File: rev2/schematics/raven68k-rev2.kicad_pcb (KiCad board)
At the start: 2 copper layers, 70 parts, among them IC1 L5970D013TR, IC2 L5970D013TR, J1 CPLD_JTAG, J2 DUART_IO, U1 MCP100-465D, U10 28C256, U11 28C256, U2 68010D, U3 XC9572XL-TQ100, U4 68681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

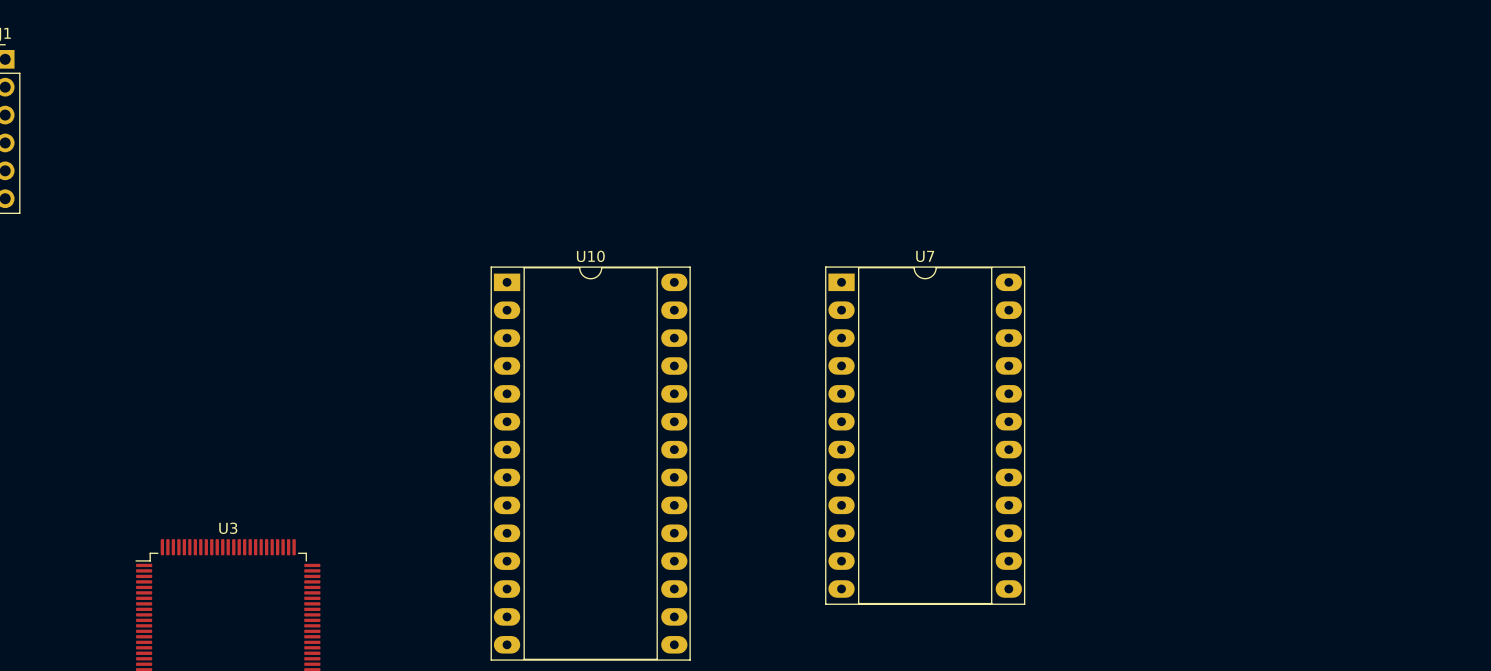
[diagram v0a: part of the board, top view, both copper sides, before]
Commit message: Fixed Bus connections. Added SIMM control connections to the CPLD. Added missing symbols from rev1 library. Cleaned up some SRAM related control signals that are no longer needed.
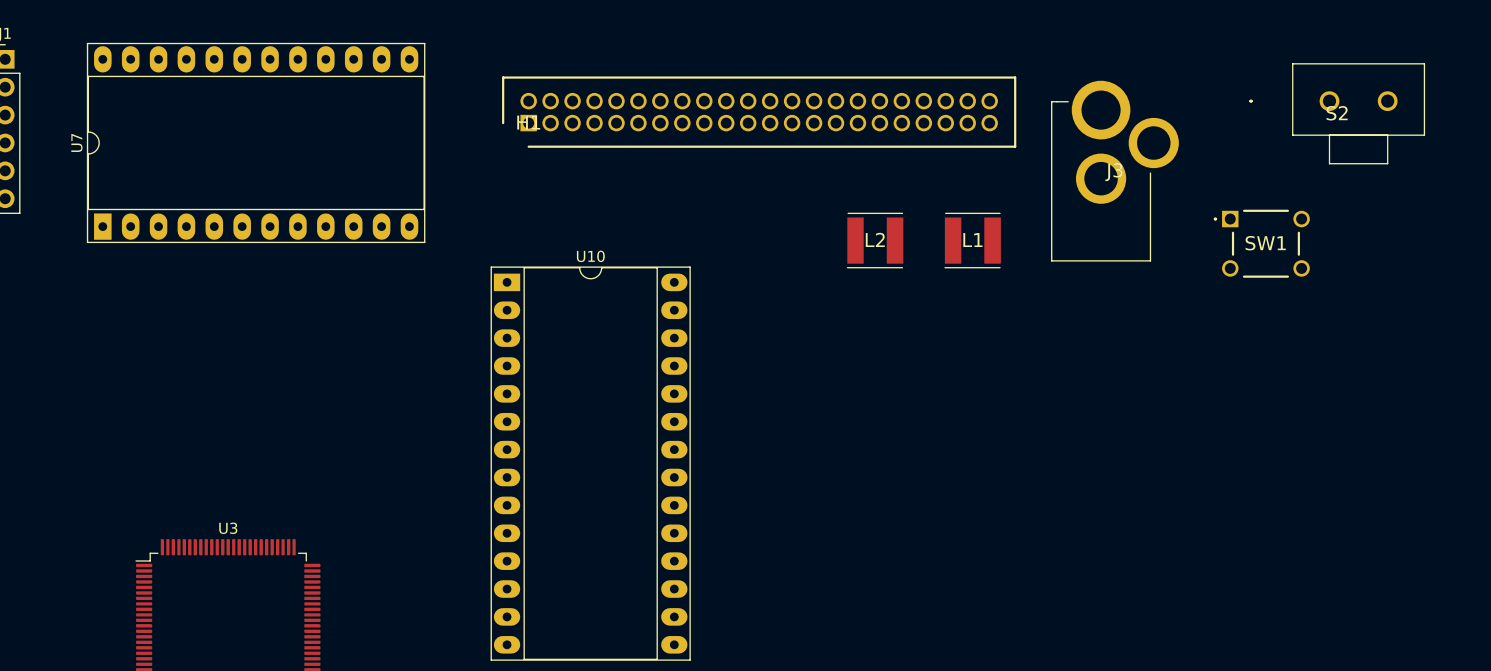
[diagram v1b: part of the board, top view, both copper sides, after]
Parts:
- added H1: IDE-44-PIN, raven68k-rev1:SHDR44W55P200_2X22_4665X630X640P, F.Cu at (98.5, 23.6)
- added J3: RAPC722BK, raven68k-rev1:RAPC722BK, F.Cu at (150.6, 22.4)
- added L1: SRN5040TA-101K, raven68k-rev1:SRN5040TA101K, F.Cu at (139.0, 34.3)
- added L2: SRN5040TA-101K, raven68k-rev1:SRN5040TA101K, F.Cu at (130.1, 34.3)
- added S2: POWER_SW, raven68k-rev1:GPTS203212B, F.Cu at (171.4, 21.6)
- added SW1: RESET_SW, raven68k-rev1:TS0266170BK160SCRD, F.Cu at (162.4, 32.3)
- moved U7 67.5 mm to (59.7, 33.0), turned to 90 degrees
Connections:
- U3 pad 10: unconnected-(U3-P10-Pad10) -> /MA3
- U3 pad 11: unconnected-(U3-P11-Pad11) -> /MA4
- U3 pad 12: unconnected-(U3-P12-Pad12) -> /MA5
- U3 pad 32: unconnected-(U3-P32-Pad32) -> ~{UDS}
- U3 pad 33: ~{RAM_LCE} -> ~{ROM_UCE}
- U3 pad 35: unconnected-(U3-P35-Pad35) -> ~{OE}
- U3 pad 37: unconnected-(U3-P37-Pad37) -> ~{AS}
- U3 pad 39: ~{RAM_UCE} -> ~{RESET}
- U3 pad 41: unconnected-(U3-P41-Pad41) -> ~{CPU_DTACK}
- U3 pad 42: unconnected-(U3-P42-Pad42) -> ~{DUART_CS}
- U3 pad 49: unconnected-(U3-P49-Pad49) -> ~{DUART_DTACK}
- U3 pad 50: unconnected-(U3-P50-Pad50) -> ~{IDE_CS2}
- U3 pad 52: unconnected-(U3-P52-Pad52) -> A1
- U3 pad 53: unconnected-(U3-P53-Pad53) -> A2
- U3 pad 54: unconnected-(U3-P54-Pad54) -> A3
- U3 pad 55: unconnected-(U3-P55-Pad55) -> A4
- U3 pad 56: unconnected-(U3-P56-Pad56) -> A5
- U3 pad 58: unconnected-(U3-P58-Pad58) -> A6
- U3 pad 59: ~{UDS} -> A7
- U3 pad 6: unconnected-(U3-P6-Pad6) -> /MA0
- U3 pad 60: ~{OE} -> A8
- U3 pad 61: ~{AS} -> A9
- U3 pad 63: ~{RESET} -> A10
- U3 pad 64: A20 -> A11
- U3 pad 65: A21 -> A12
- U3 pad 66: A22 -> A13
- U3 pad 67: A1 -> A14
- U3 pad 68: A23 -> A15
- U3 pad 70: A2 -> A16
- U3 pad 71: A3 -> A17
- U3 pad 72: A4 -> A18
- U3 pad 74: ~{CPU_DTACK} -> A19
- U3 pad 76: ~{DUART_CS} -> A20
- U3 pad 77: ~{DUART_DTACK} -> A21
- U3 pad 78: unconnected-(U3-P78-Pad78) -> A22
- U3 pad 79: unconnected-(U3-P79-Pad79) -> A23
- U3 pad 8: unconnected-(U3-P8-Pad8) -> /MA1
- U3 pad 81: unconnected-(U3-P81-Pad81) -> /CAS0
- U3 pad 82: unconnected-(U3-P82-Pad82) -> /CAS1
- U3 pad 85: unconnected-(U3-P85-Pad85) -> /CAS2
- U3 pad 86: unconnected-(U3-P86-Pad86) -> /CAS3
- U3 pad 87: unconnected-(U3-P87-Pad87) -> /MA6
- U3 pad 89: unconnected-(U3-P89-Pad89) -> /RAS2
- U3 pad 9: unconnected-(U3-P9-Pad9) -> /MA2
- U3 pad 90: unconnected-(U3-P90-Pad90) -> /RAS3
- U3 pad 91: unconnected-(U3-P91-Pad91) -> /MA7
- U3 pad 92: unconnected-(U3-P92-Pad92) -> /MA8
- U3 pad 93: unconnected-(U3-P93-Pad93) -> /MA9
- U3 pad 94: unconnected-(U3-P94-Pad94) -> /MA10
- U3 pad 95: unconnected-(U3-P95-Pad95) -> /MA11
- U3 pad 96: ~{ROM_UCE} -> /RAS0
- U3 pad 97: unconnected-(U3-P97-Pad97) -> /RAS1

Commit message: Added upper two bytes to SIMM connection. Updated the PCB at the same time.
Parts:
- moved U1 153.8 mm to (105.4, 30.5)
- moved D5 147.2 mm to (146.1, 49.5)
- moved R6 144.3 mm to (44.7, 130.8), turned to 90 degrees
- moved R1 135.2 mm to (126.3, 107.2)
- moved R2 135.2 mm to (126.3, 110.5)
- moved R3 135.2 mm to (126.3, 113.8)
- moved R4 135.2 mm to (126.3, 117.1)
- moved R5 135.2 mm to (126.3, 120.4)
- moved C1 135.2 mm to (120.4, 107.2)
- moved C2 135.2 mm to (120.4, 110.6)
- moved C28 135.2 mm to (120.4, 120.7)
- moved C3 135.2 mm to (120.4, 114.0)
- moved C4 135.2 mm to (120.4, 117.3)
- moved R10 129.0 mm to (158.5, 57.7)
- moved R21 129.0 mm to (158.5, 61.0)
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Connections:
- net /CAS0 renamed CAS0
- net /CAS1 renamed CAS1
- net /CAS2 renamed CAS2
- net /CAS3 renamed CAS3
- net /MA0 renamed MA0
- net /MA1 renamed MA1
- net /MA10 renamed MA10
- net /MA11 renamed MA11
- net /MA2 renamed MA2
- net /MA3 renamed MA3
- net /MA4 renamed MA4
- net /MA5 renamed MA5
- net /MA6 renamed MA6
- net /MA7 renamed MA7
- net /MA8 renamed MA8
- net /MA9 renamed MA9
- net /RAS0 renamed RAS0
- net /RAS1 renamed RAS1
- net /RAS2 renamed RAS2
- net /RAS3 renamed RAS3

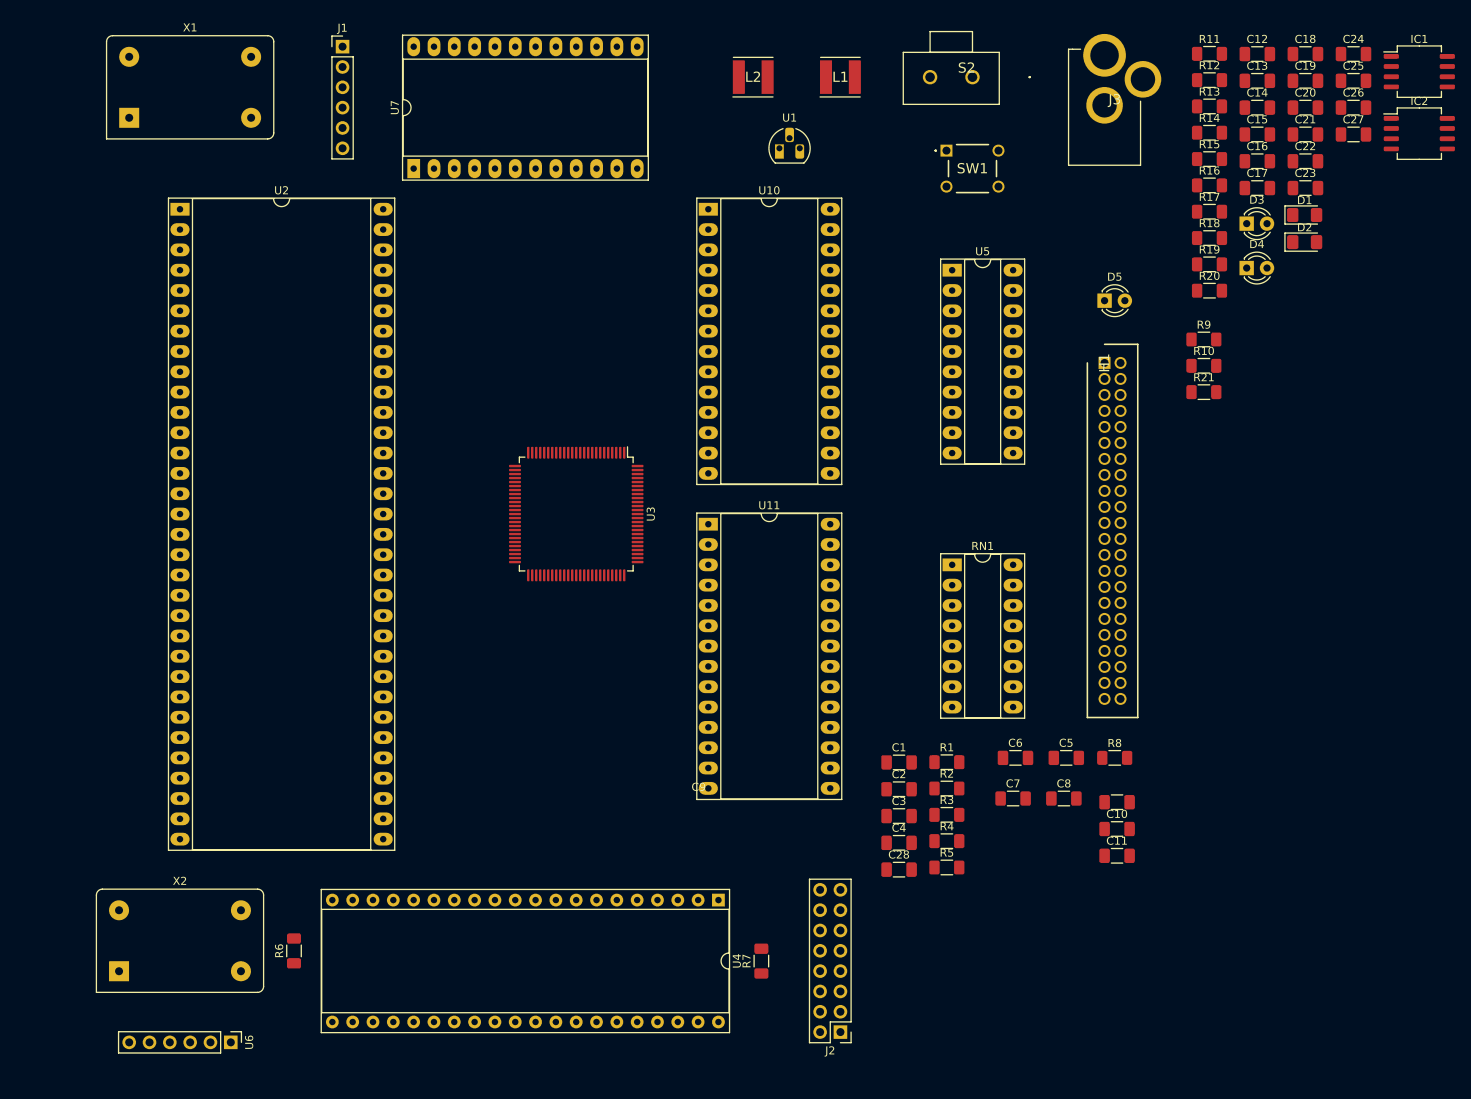
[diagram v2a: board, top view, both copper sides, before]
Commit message: Added SIMM footprint and Raven logo. Did initial PCB component placement and routing using autorouter. Still needs to be checked before ordering PCBs to verify on an actual hardware.
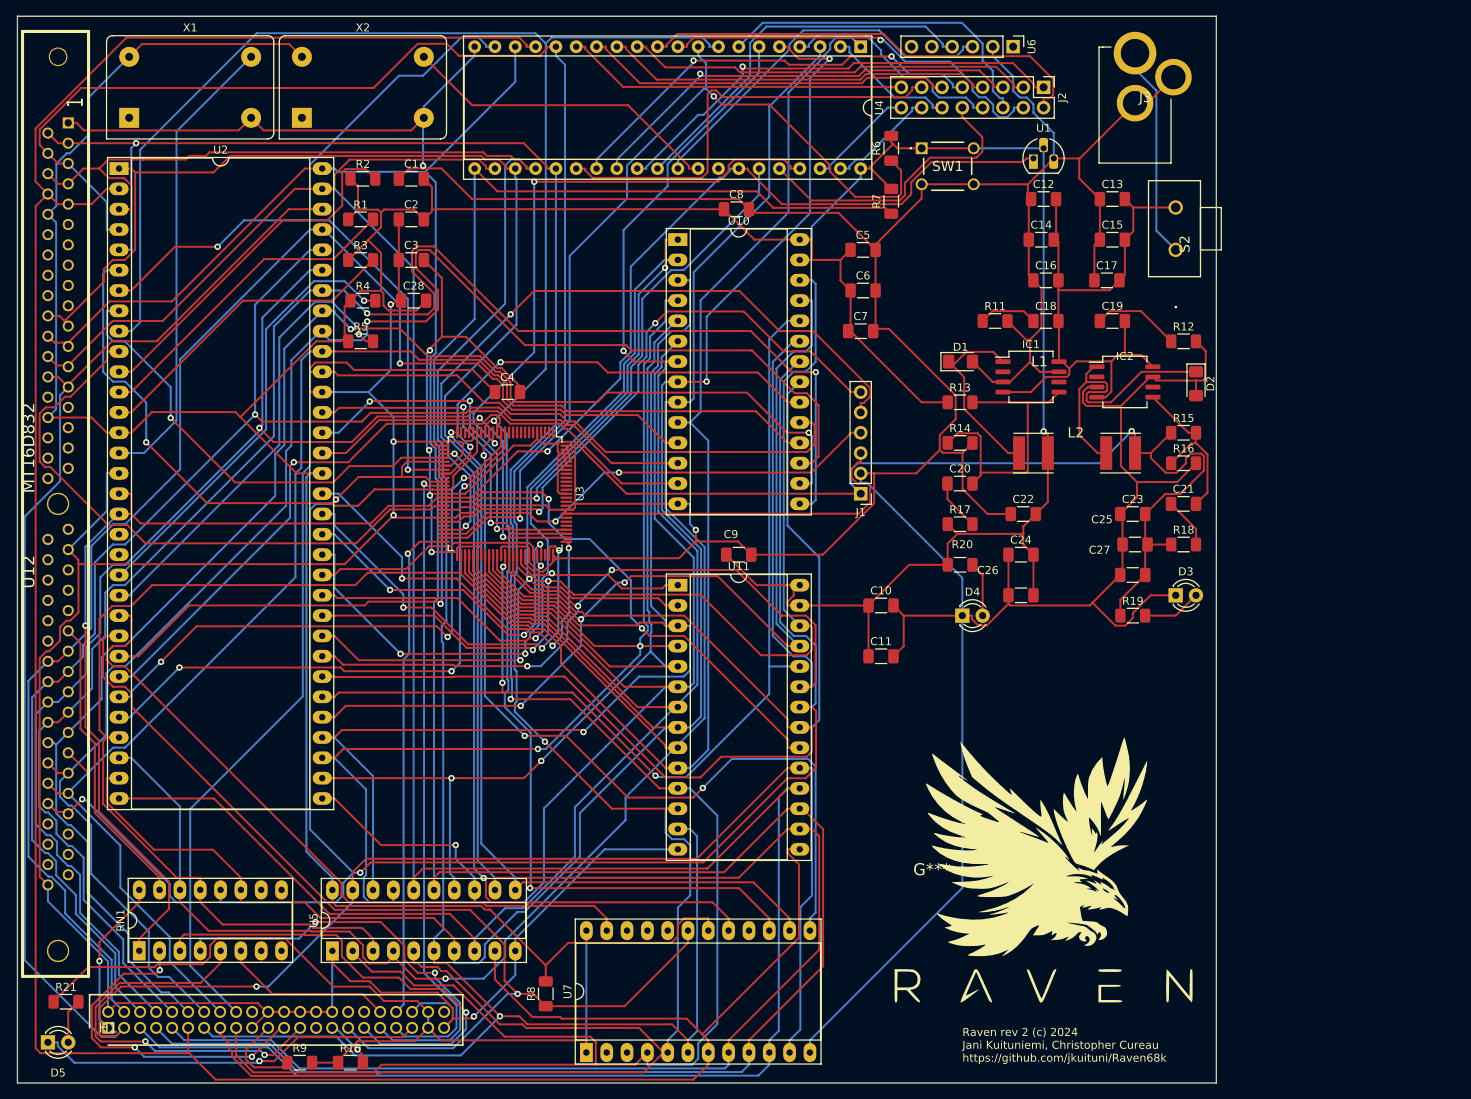
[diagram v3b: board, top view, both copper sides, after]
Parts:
- added G***: LOGO, raven68k-rev1:Raven_Logo, F.Cu at (138.4, 120.7)
- added U12: MT16D832, KISS68030 Lib:DRAM-72-2021, F.Cu at (15.2, 74.9)
- moved D5 161.4 mm to (14.0, 142.2)
- moved R21 161.4 mm to (16.2, 137.2)
- moved U6 158.3 mm to (134.6, 17.8)
- moved H1 149.7 mm to (21.5, 140.4), turned to 0 degrees
- moved R9 144.7 mm to (45.4, 144.8)
- moved R10 137.7 mm to (51.8, 144.8)
- moved R6 125.1 mm to (119.4, 30.5)
- moved J2 120.8 mm to (138.4, 22.9), turned to -90 degrees
- moved U5 115.1 mm to (49.5, 130.8), turned to 90 degrees
- moved U7 112.6 mm to (81.3, 143.5)
- moved RN1 112.5 mm to (25.4, 130.8), turned to 90 degrees
- moved X2 109.1 mm to (45.7, 26.7)
- moved U4 108.1 mm to (115.6, 17.8)
- moved R2 105.5 mm to (53.3, 34.3)
- moved R3 100.9 mm to (53.1, 44.5)
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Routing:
- net GND: track 0.00 -> 944.1 mm, vias 0 -> 6
- net +5V: track 0.00 -> 677.4 mm, vias 0 -> 1
- net D3: track 0.00 -> 350.6 mm
- net D6: track 0.00 -> 335.2 mm
- net D1: track 0.00 -> 334.3 mm, vias 0 -> 1
- net D5: track 0.00 -> 333.5 mm
- net D4: track 0.00 -> 324.2 mm
- net D7: track 0.00 -> 319.6 mm, vias 0 -> 1
- net D0: track 0.00 -> 315.8 mm, vias 0 -> 2
- net D2: track 0.00 -> 290.7 mm, vias 0 -> 1
- net A1: track 0.00 -> 265.0 mm
- net R~{W}: track 0.00 -> 250.4 mm, vias 0 -> 2
- net A3: track 0.00 -> 246.8 mm, vias 0 -> 2
- net A2: track 0.00 -> 244.5 mm, vias 0 -> 1
- net A4: track 0.00 -> 231.1 mm, vias 0 -> 1
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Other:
- board outline added: 149.9 x 133.3 mm
- board text added: "Raven rev 2 (c) 2024 Jani Kuituniemi, Christopher Cureau https://github.com/jkuituni/Raven68k"
